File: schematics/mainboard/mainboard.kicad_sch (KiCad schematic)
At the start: 101 parts, among them J1 SD_Card_Receptacle, J2 LCD_CONN, J3 USB_C_Receptacle_USB2.0_16P, J4 BATTERY_CONN, J5 527461671, J6 SPEAKER_CONN, J9 AudioJack3, P1 1-1473005-4, SW1 SW_SPST, U1 AMS1117-3.3, U2 AMS1117-3.3, U3 MAX3421EETJ_T, U5 AMS1117-1.8, U6 TPS63002, U7 BQ24072RGT, U9 TPS22917DBV, Y1 12MHz

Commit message: Revision 1 of mainboard finished and ordered from JLCPCB.
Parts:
- removed SW1: SW_SPST, Connector_PinHeader_2.54mm:PinHeader_1x02_P2.54mm_Vertical, symbol Switch:SW_SPST
- added C42: 10uF, Capacitor_Tantalum_SMD:CP_EIA-3216-18_Kemet-A, symbol Device:C_Polarized
- added C43: 47uF, Capacitor_Tantalum_SMD:CP_EIA-3216-18_Kemet-A, symbol Device:C_Polarized
- added R18, R19: 10k, Resistor_SMD:R_0603_1608Metric_Pad0.98x0.95mm_HandSolder, symbol Device:R
- added S1: SSSS811101, SSSS811101:SW_SSSS811101, symbol SSSS811101:SSSS811101
- added U10: PCA9555PW, Package_SO:TSSOP-24_4.4x7.8mm_P0.65mm, symbol Interface_Expansion:PCA9555PW
- C18: value 0.1u -> 0.1uF
- C40: footprint Capacitor_SMD:CP_Elec_5x5.3 -> Capacitor_Tantalum_SMD:CP_EIA-3216-18_Kemet-A; LCSC (none) -> C7190
- C41: value 200pF -> 500pF
- C5: value 10uF -> 1uF; footprint Capacitor_SMD:C_0805_2012Metric_Pad1.18x1.45mm_HandSolder -> Capacitor_SMD:C_0805_2012Metric; LCSC C1713 -> (none)
- R26: value 1k -> 68
- R27: value 1k -> 30
- R29: value 57k -> 10k
- R3: value 1.18k -> 1.2k
- R32: value ~ -> NC
- R4: value 1.13k -> 1.2k
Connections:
- net 3V3: now also C23.1, C24.1, C26.1, C33.1, C35.1, C37.1, C40.1, J5.15, R17.1, U5.3 (VI), U8.17 (AVDD), U8.2 (IOVDD), U8.28 (HPVDD), C42.1, R18.2, U10.24 (VDD); no longer J5.P2
- net AUDIO_BCLK: now also P1.66; no longer P1.68
- net AUDIO_DIN: now also P1.70; no longer P1.64
- net AUDIO_MCLK: now also P1.64; no longer P1.70
- net AUDIO_WCLK: now also P1.68; no longer P1.66
- net GND: now also C5.1, J5.P1, J5.P2, C42.2, C43.2, R19.2, U10.12 (VSS), U10.2 (A1), U10.21 (A0), U10.3 (A2); no longer C41.1, C5.2
- net I2C_SCL: now also P1.60, R34.2, U10.22 (SCL); no longer P1.58, R33.2
- net I2C_SDA: now also P1.58, R33.2, U10.23 (SDA); no longer P1.60, R34.2
- net at C28.2, R26.1, R27.1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: now also C41.1, S1.2
- net at U9.3 (ON): now also R19.1, S1.1
- net at U3.22 (VBCOMP): now also C5.2
- net KEYPAD_INTERRUPT: now reaches P1.155
- net KEYPAD_INTERRUPT: now also R18.1, U10.1 (~{INT})
- net 3V3_AUDIO renamed 3V3_LCD
- net 3V3_LCD: now also C43.1; no longer C23.1, C24.1, C26.1, C33.1, C35.1, C37.1, C40.1, C5.1, R17.1, U5.3 (VI), U8.17 (AVDD), U8.2 (IOVDD), U8.28 (HPVDD)
- net HIO_BTN_A: no longer names the net of J5.6, R10.1
- net HIO_BTN_A: now also U10.8 (IO0_4); no longer P1.86
- net HIO_BTN_B: no longer names the net of J5.7, R14.1
- net HIO_BTN_B: now also U10.9 (IO0_5); no longer P1.88
- net HIO_BTN_C: no longer names the net of J5.8, R11.1
- net HIO_BTN_C: now also U10.10 (IO0_6); no longer P1.90
- net HIO_BTN_D: no longer names the net of J5.9, R15.1
- net HIO_BTN_D: now also U10.11 (IO0_7); no longer P1.92
- net HIO_BTN_RESET: no longer names the net of J5.11, R20.1
- net HIO_BTN_RESET: now also U10.14 (IO1_1); no longer P1.96
- net HIO_BTN_X: no longer names the net of J5.10, R16.1
- net HIO_BTN_X: now also U10.13 (IO1_0); no longer P1.94
- net HIO_DPAD_E: no longer names the net of J5.5, R13.1
- net HIO_DPAD_E: now also U10.7 (IO0_3); no longer P1.84
- net HIO_DPAD_N: no longer names the net of J5.2, R8.1
- net HIO_DPAD_N: now also U10.4 (IO0_0); no longer P1.78
- net HIO_DPAD_S: no longer names the net of J5.3, R12.1
- net HIO_DPAD_S: now also U10.5 (IO0_1); no longer P1.80
- net HIO_DPAD_W: no longer names the net of J5.4, R9.1
- net HIO_DPAD_W: now also U10.6 (IO0_2); no longer P1.82
- net VOL/MICDET: no longer names the net of U8.11 (VOL/MICDET)
- no-connect marks 77 -> 103
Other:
- note added: "I2C address 0x40"
- note added: "TLV320 I2C address 0x18"
- note added: "Trackball I2C address 0x0A"
- moved on the sheet: C41, J5, P1, R10, R11, R12, R13, R14, R15, R16, R20, R33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

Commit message: Incorrect part number and also incorrect footprint fixed. Another attempt at JLCPCB.
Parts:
- U3: footprint MAX:QFN50P500X500X80-33N -> MAX2:QFP50P700X700X120-32N
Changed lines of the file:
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@@
 			)
 		)
-		(property "Footprint" "MAX:QFN50P500X500X80-33N"
+		(property "Footprint" "MAX2:QFP50P700X700X120-32N"
 			(at 80.01 97.79 0)
 			(effects

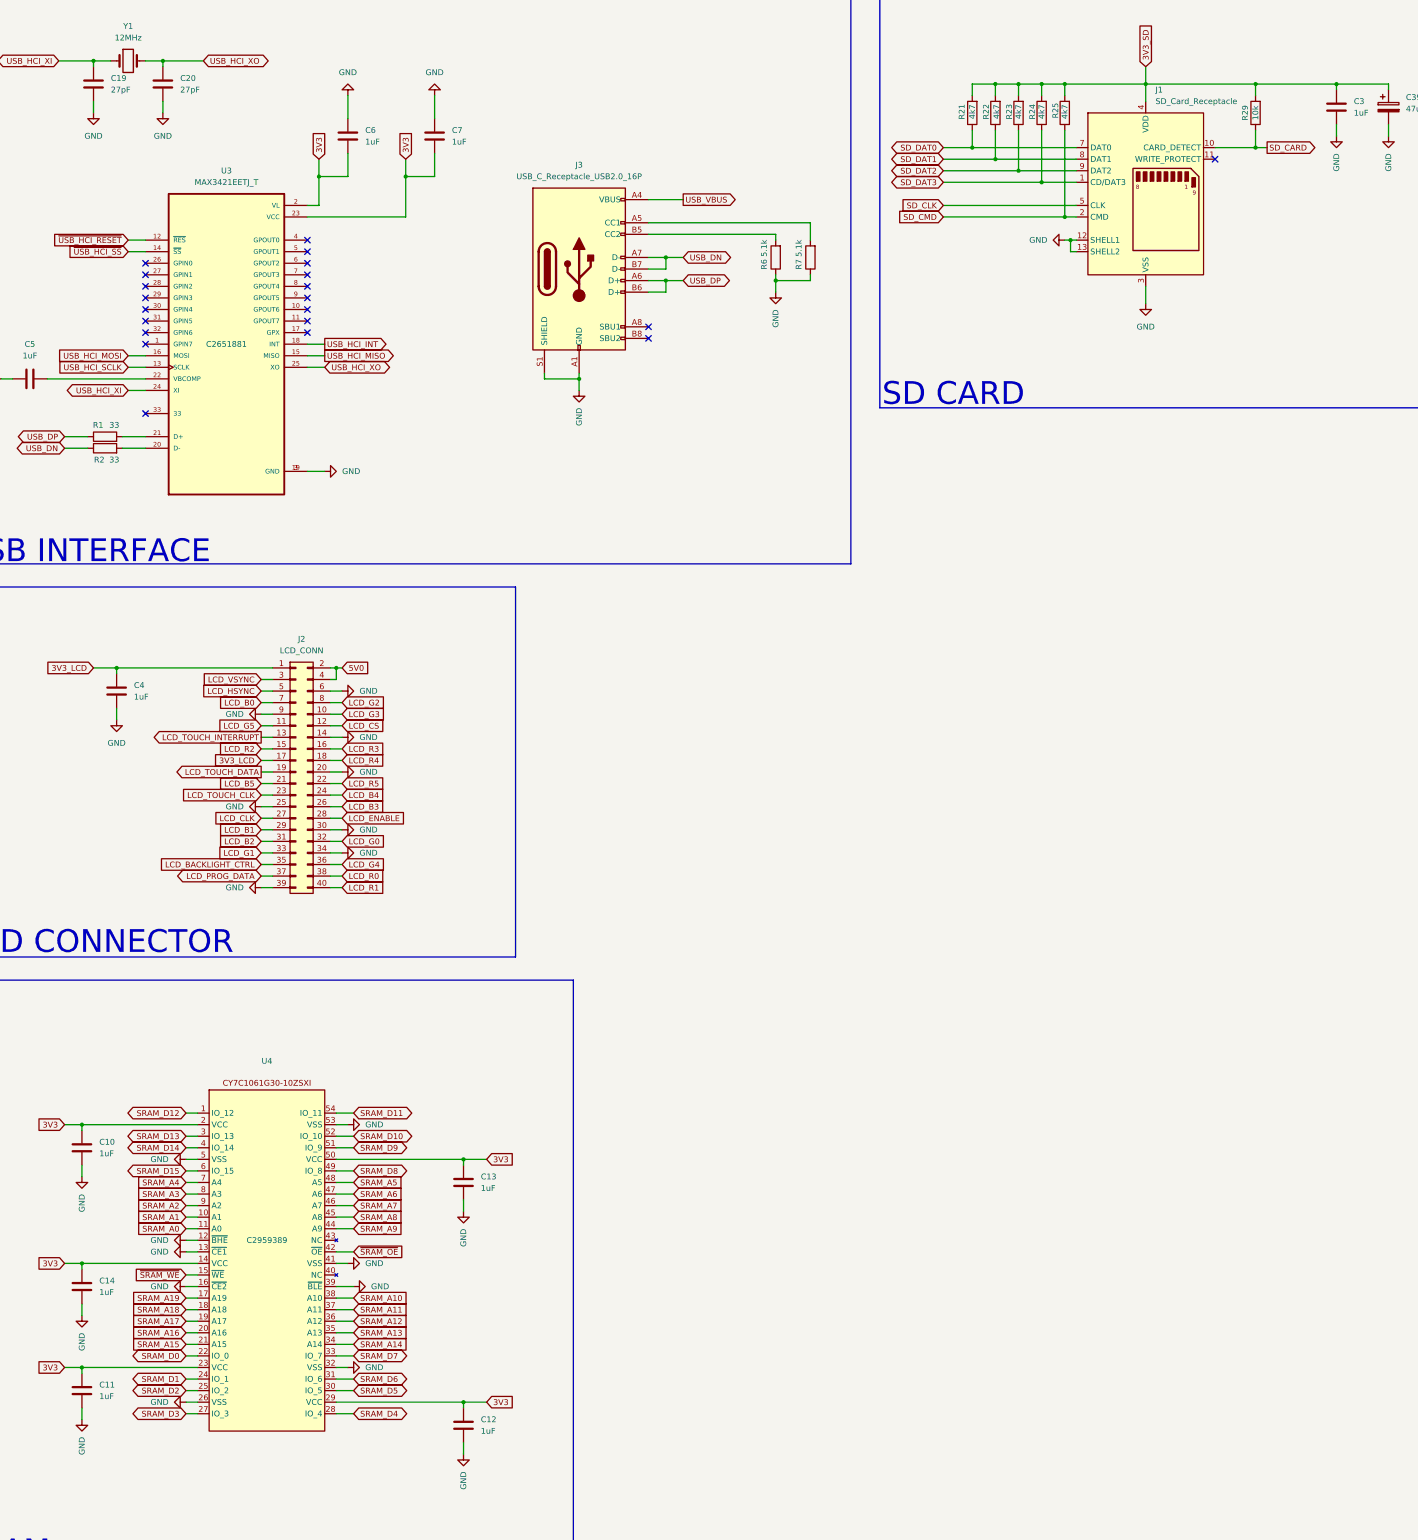
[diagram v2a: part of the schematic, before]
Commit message: Actual mainboard hardware work; display, vram, audio, sd card etc.
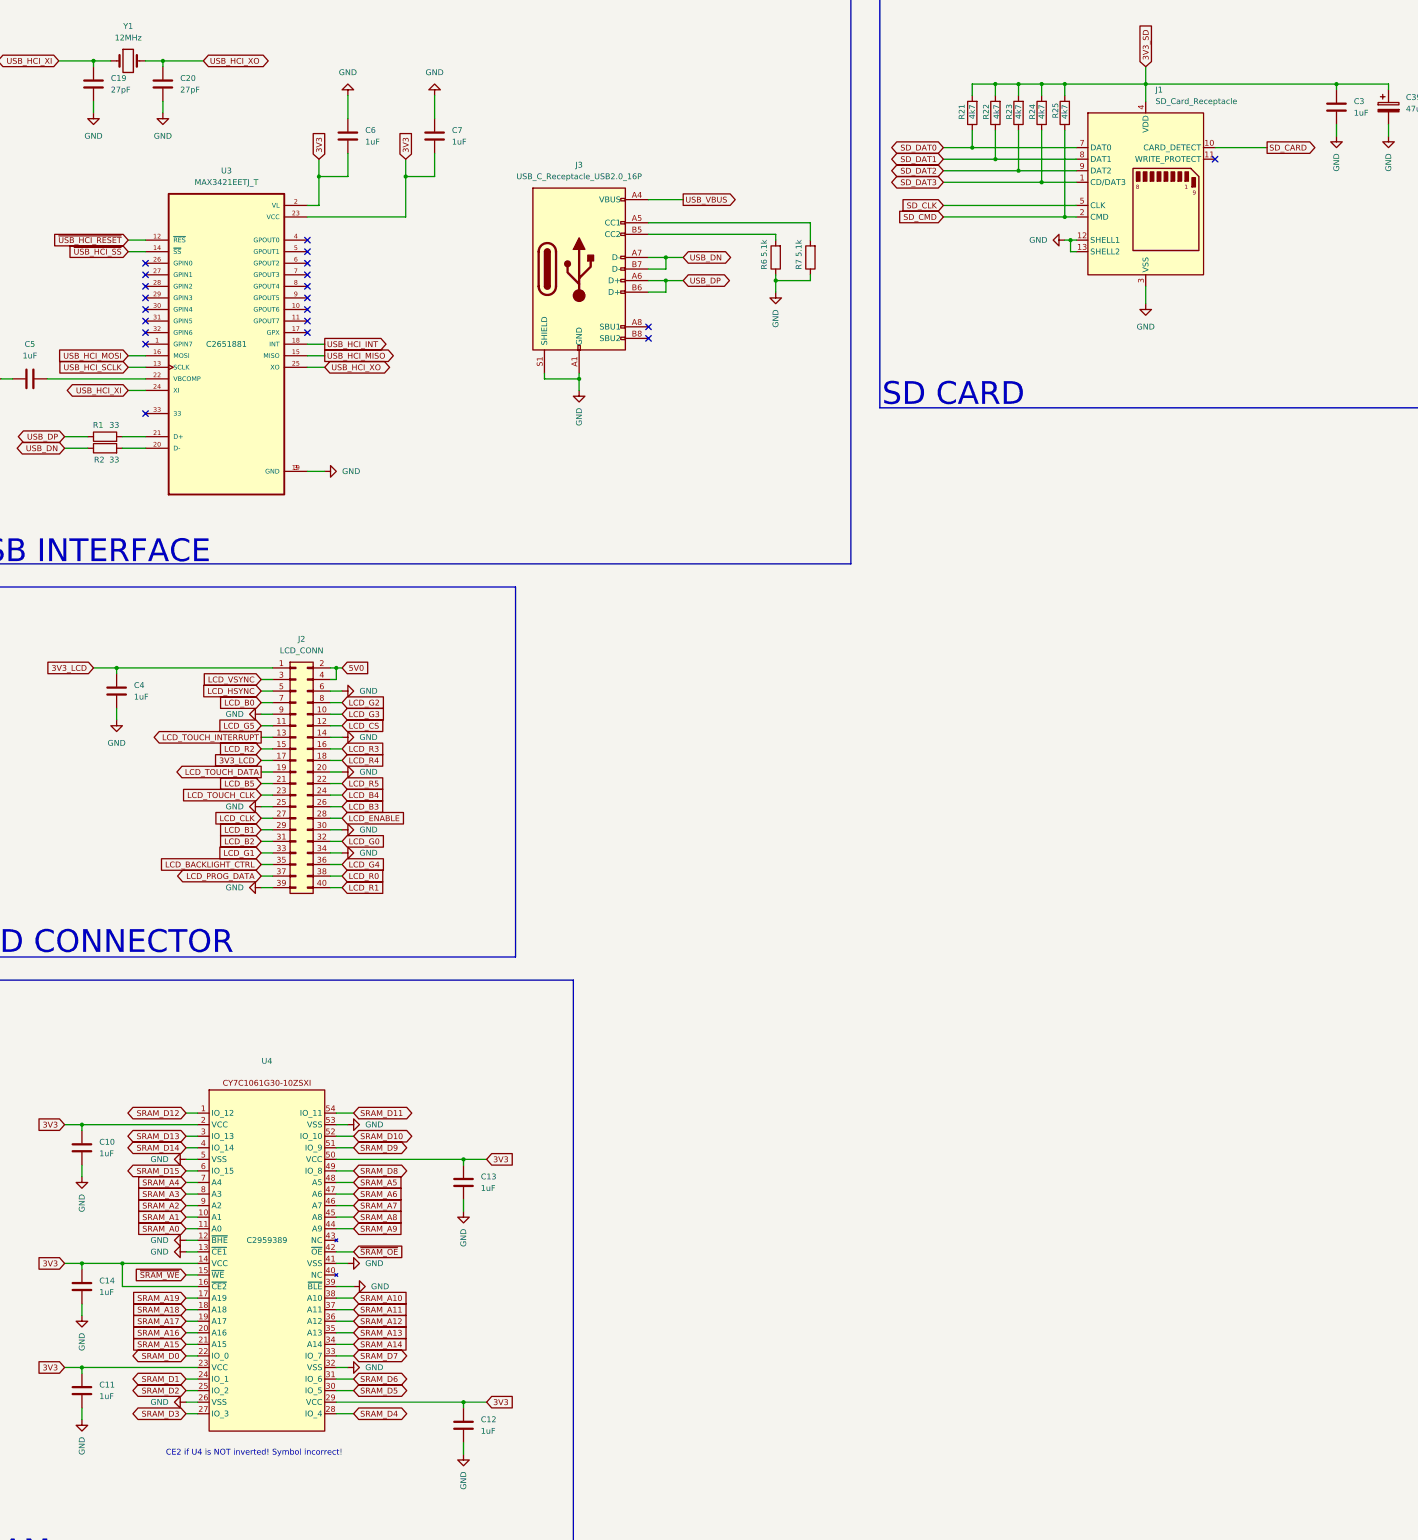
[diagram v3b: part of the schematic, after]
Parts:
- removed R29: 10k, Resistor_SMD:R_0603_1608Metric_Pad0.98x0.95mm_HandSolder, symbol Device:R
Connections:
- net 3V3: now also U4.16 (~{CE2})
- net GND: no longer U4.16 (~{CE2})
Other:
- note added: "CE2 if U4 is NOT inverted! Symbol incorrect!"
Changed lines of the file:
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@@
 		)
 	)
+	(text "CE2 if U4 is NOT inverted! Symbol incorrect!"
+		(exclude_from_sim no)
+		(at 86.106 341.376 0)
+		(effects
+			(font
+				(size 1.27 1.27)
+			)
+		)
+	)
 	(text "Trackball I2C address 0x0A"
 		(exclude_from_sim no)
@@
 	)
 	(junction
+		(at 57.15 299.72)
+		(diameter 0)
+		(color 0 0 0 0)
+	)
+	(junction
 		(at 363.22 232.41)
 		(diameter 0)
@@
 	)
 	(junction
-		(at 306.07 40.64)
-		(diameter 0)
-		(color 0 0 0 0)
-	)
-	(junction
 		(at 721.36 297.18)
 		(diameter 0)
@@
 	)
 	(junction
-		(at 306.07 54.61)
-		(diameter 0)
-		(color 0 0 0 0)
-	)
-	(junction
 		(at 254 40.64)
 		(diameter 0)
@@
 	(wire
 		(pts
-			(xy 121.92 453.39) (xy 121.92 455.93)
+			(xy 57.15 304.8) (xy 73.66 304.8)
 		)
 		(stroke
@@
 	(wire
 		(pts
-			(xy 436.88 289.56) (xy 430.53 289.56)
+			(xy 121.92 453.39) (xy 121.92 455.93)
 		)
 		(stroke
@@
 	(wire
 		(pts
-			(xy 281.94 40.64) (xy 306.07 40.64)
+			(xy 436.88 289.56) (xy 430.53 289.56)
 		)
 		(stroke
@@
 	(wire
 		(pts
-			(xy 71.12 304.8) (xy 73.66 304.8)
-		)
-		(stroke
-			(width 0)
-			(type default)
-		)
-	)
-	(wire
-		(pts
 			(xy 396.24 430.53) (xy 400.05 430.53)
 		)
@@
 	(wire
 		(pts
-			(xy 48.26 299.72) (xy 73.66 299.72)
+			(xy 48.26 299.72) (xy 57.15 299.72)
 		)
 		(stroke
@@
 	(wire
 		(pts
-			(xy 306.07 40.64) (xy 306.07 43.18)
-		)
-		(stroke
-			(width 0)
-			(type default)
-		)
-	)
-	(wire
-		(pts
 			(xy 396.24 486.41) (xy 398.78 486.41)
 		)
@@
 	(wire
 		(pts
+			(xy 57.15 304.8) (xy 57.15 299.72)
+		)
+		(stroke
+			(width 0)
+			(type default)
+		)
+	)
+	(wire
+		(pts
 			(xy 396.24 369.57) (xy 397.51 369.57)
 		)
@@
 	(wire
 		(pts
-			(xy 297.18 54.61) (xy 306.07 54.61)
+			(xy 297.18 54.61) (xy 308.61 54.61)
 		)
 		(stroke
@@
 	(wire
 		(pts
-			(xy 306.07 50.8) (xy 306.07 54.61)
+			(xy 712.47 114.3) (xy 702.31 114.3)
 		)
 		(stroke
@@
 	(wire
 		(pts
-			(xy 712.47 114.3) (xy 702.31 114.3)
+			(xy 40.64 105.41) (xy 62.23 105.41)
 		)
 		(stroke
@@
 	(wire
 		(pts
-			(xy 40.64 105.41) (xy 62.23 105.41)
+			(xy 759.46 359.41) (xy 759.46 356.87)
 		)
 		(stroke
@@
 	(wire
 		(pts
-			(xy 759.46 359.41) (xy 759.46 356.87)
+			(xy 759.46 182.88) (xy 759.46 185.42)
 		)
 		(stroke
@@
 	(wire
 		(pts
-			(xy 759.46 182.88) (xy 759.46 185.42)
+			(xy 132.08 285.75) (xy 132.08 288.29)
 		)
 		(stroke
@@
 	(wire
 		(pts
-			(xy 132.08 285.75) (xy 132.08 288.29)
+			(xy 636.27 69.85) (xy 647.7 69.85)
 		)
 		(stroke
@@
 	(wire
 		(pts
-			(xy 636.27 69.85) (xy 647.7 69.85)
+			(xy 363.22 280.67) (xy 365.76 280.67)
 		)
 		(stroke
@@
 	(wire
 		(pts
-			(xy 363.22 280.67) (xy 365.76 280.67)
+			(xy 57.15 299.72) (xy 73.66 299.72)
 		)
 		(stroke
@@
 	(wire
 		(pts
-			(xy 306.07 40.64) (xy 323.85 40.64)
+			(xy 281.94 40.64) (xy 323.85 40.64)
 		)
 		(stroke
@@
 	(wire
 		(pts
-			(xy 306.07 54.61) (xy 308.61 54.61)
-		)
-		(stroke
-			(width 0)
-			(type default)
-		)
-	)
-	(wire
-		(pts
 			(xy 430.53 31.75) (xy 430.53 35.56)
 		)
@@
 	)
 	(symbol
-		(lib_id "Device:R")
-		(at 306.07 46.99 180)
-		(unit 1)
-		(exclude_from_sim no)
-		(in_bom yes)
-		(on_board yes)
-		(dnp no)
-		(property "Reference" "R29"
-			(at 303.784 46.99 90)
-			(effects
-				(font
-					(size 1.27 1.27)
-				)
-			)
-		)
-		(property "Value" "10k"
-			(at 306.07 46.99 90)
-			(effects
-				(font
-					(size 1.27 1.27)
-				)
-			)
-		)
-		(property "Footprint" "Resistor_SMD:R_0603_1608Metric_Pad0.98x0.95mm_HandSolder"
-			(at 307.848 46.99 90)
-			(effects
-				(font
-					(size 1.27 1.27)
-				)
-				(hide yes)
-			)
-		)
-		(property "Datasheet" "~"
-			(at 306.07 46.99 0)
-			(effects
-				(font
-					(size 1.27 1.27)
-				)
-				(hide yes)
-			)
-		)
-		(property "Description" "Resistor"
-			(at 306.07 46.99 0)
-			(effects
-				(font
-					(size 1.27 1.27)
-				)
-				(hide yes)
-			)
-		)
-		(pin "1"
-		)
-		(pin "2"
-		)
-		(instances
-			(project "mainboard"
-				(path "/cefc859f-34fb-418b-9c7c-f7e62c11b64f"
-					(reference "R29")
-					(unit 1)
-				)
-			)
-		)
-	)
-	(symbol
 		(lib_id "Device:C_Polarized")
 		(at 430.53 39.37 0)
@@
 					(unit 1)
 				)
-			)
-		)
-	)
-	(symbol
-		(lib_id "power:GND")
-		(at 71.12 304.8 270)
-		(unit 1)
-		(exclude_from_sim no)
-		(in_bom yes)
-		(on_board yes)
-		(dnp no)
-		(property "Reference" "#PWR048"
-			(at 64.77 304.8 0)
-			(effects
-				(font
-					(size 1.27 1.27)
-				)
-				(hide yes)
-			)
-		)
-		(property "Value" "GND"
-			(at 67.31 304.8001 90)
-			(effects
-				(font
-					(size 1.27 1.27)
-				)
-				(justify right)
-			)
-		)
-		(property "Footprint" ""
-			(at 71.12 304.8 0)
-			(effects
-				(font
-					(size 1.27 1.27)
-				)
-				(hide yes)
-			)
-		)
-		(property "Datasheet" ""
-			(at 71.12 304.8 0)
-			(effects
-				(font
-					(size 1.27 1.27)
-				)
-				(hide yes)
-			)
-		)
-		(property "Description" "Power symbol creates a global label with name \"GND\" , ground"
-			(at 71.12 304.8 0)
-			(effects
-				(font
-					(size 1.27 1.27)
-				)
-				(hide yes)
-			)
-		)
-		(pin "1"
-		)
-		(instances
-			(project "mainboard"
-				(path "/cefc859f-34fb-418b-9c7c-f7e62c11b64f"
-					(reference "#PWR048")
-					(unit 1)
-				)

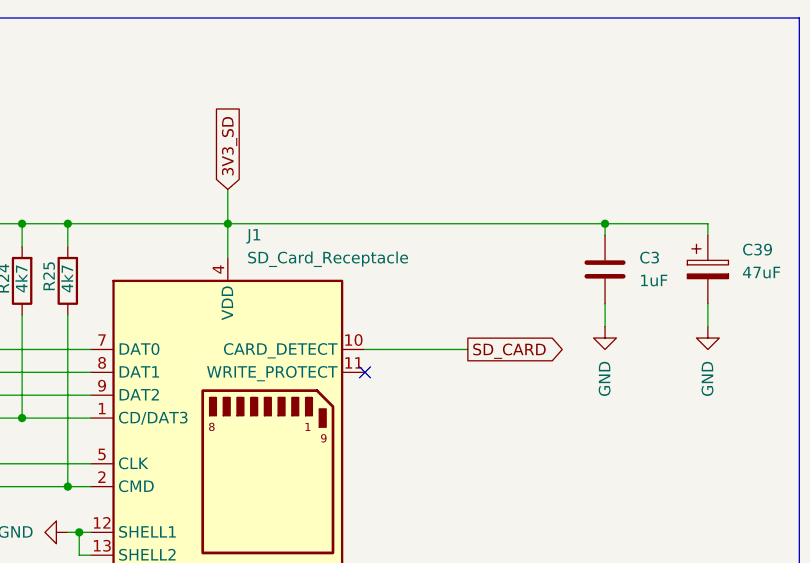
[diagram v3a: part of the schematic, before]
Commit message: Begun work on mainboard rev 2; fixed SD card and also CE pin on SRAM fixed.
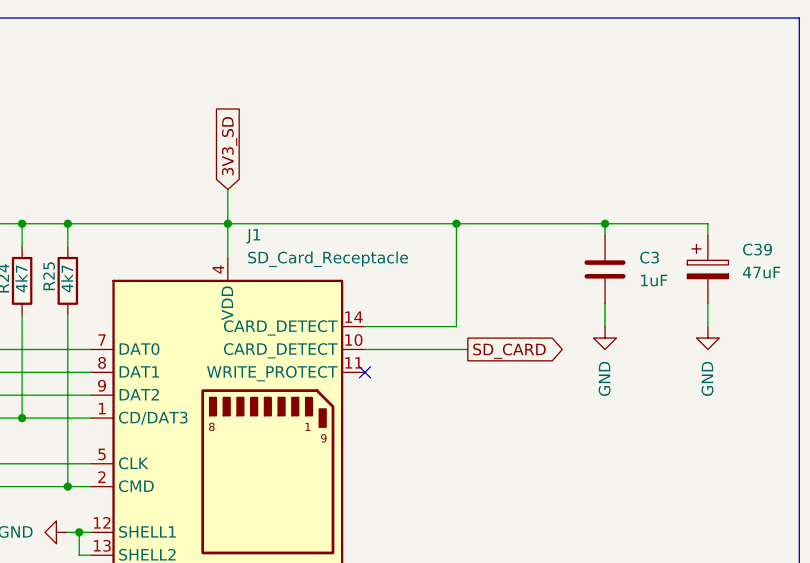
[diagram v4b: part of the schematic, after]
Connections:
- net 3V3_LCD: now also J1.14 (CARD_DETECT)
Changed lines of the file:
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@@
 	)
 	(junction
+		(at 307.34 40.64)
+		(diameter 0)
+		(color 0 0 0 0)
+	)
+	(junction
 		(at 635 367.03)
 		(diameter 0)
@@
 	(wire
 		(pts
+			(xy 297.18 52.07) (xy 307.34 52.07)
+		)
+		(stroke
+			(width 0)
+			(type default)
+		)
+	)
+	(wire
+		(pts
 			(xy 712.47 114.3) (xy 702.31 114.3)
 		)
@@
 	(wire
 		(pts
+			(xy 307.34 40.64) (xy 323.85 40.64)
+		)
+		(stroke
+			(width 0)
+			(type default)
+		)
+	)
+	(wire
+		(pts
 			(xy 396.24 285.75) (xy 400.05 285.75)
 		)
@@
 	(wire
 		(pts
-			(xy 281.94 40.64) (xy 323.85 40.64)
+			(xy 281.94 40.64) (xy 307.34 40.64)
 		)
 		(stroke
@@
 	(wire
 		(pts
+			(xy 307.34 52.07) (xy 307.34 40.64)
+		)
+		(stroke
+			(width 0)
+			(type default)
+		)
+	)
+	(wire
+		(pts
 			(xy 401.32 44.45) (xy 401.32 45.72)
 		)
@@
 		(pin "9"
 		)
+		(pin "14"
+		)
 		(instances
